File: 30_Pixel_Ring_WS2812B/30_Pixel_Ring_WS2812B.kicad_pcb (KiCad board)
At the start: 2 copper layers, 87.6 x 87.6 mm, 66 parts, among them P1 CONN_01X01, P2 CONN_01X01, P3 CONN_01X01, P4 CONN_01X01, P5 CONN_01X01, P6 CONN_01X01

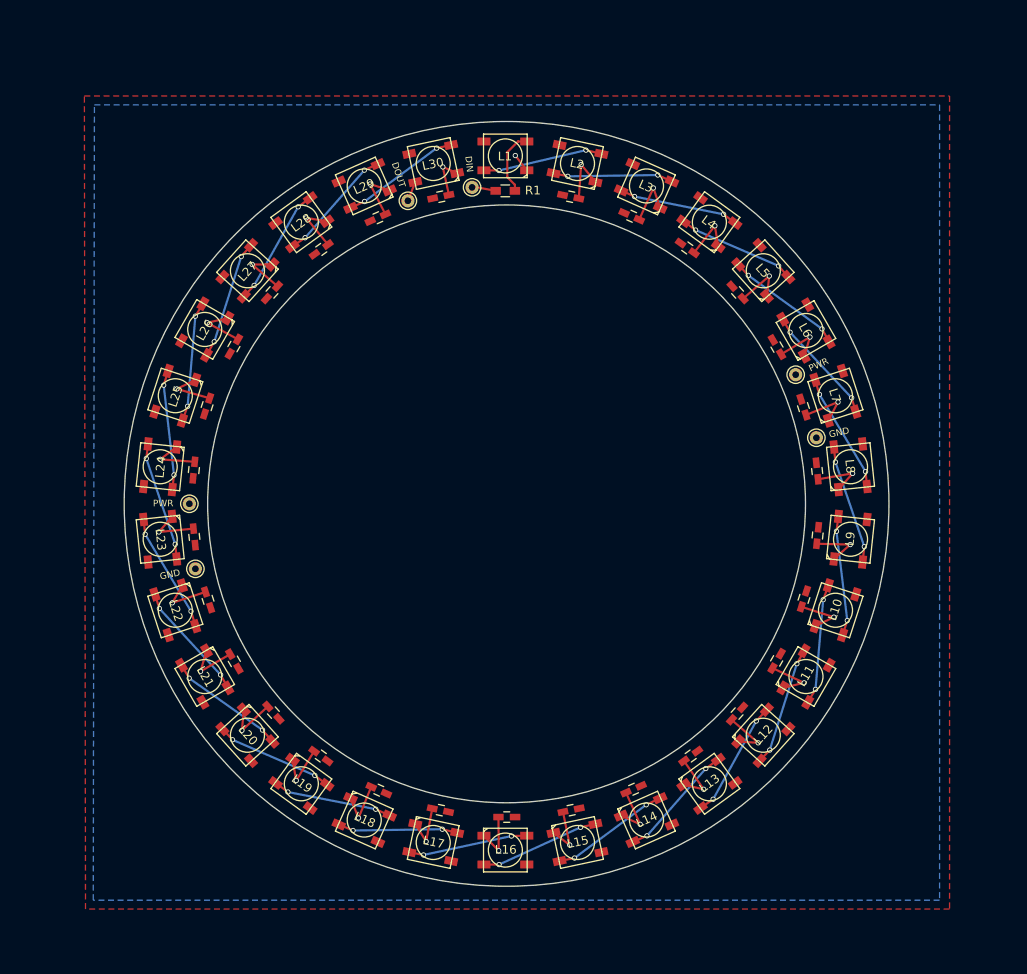
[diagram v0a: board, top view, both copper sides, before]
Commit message: 30 Pixel ring updates
Updates / refinements in preparation for nesting this ring around the 20
pixel ring and sending for fabrication through OSH Park
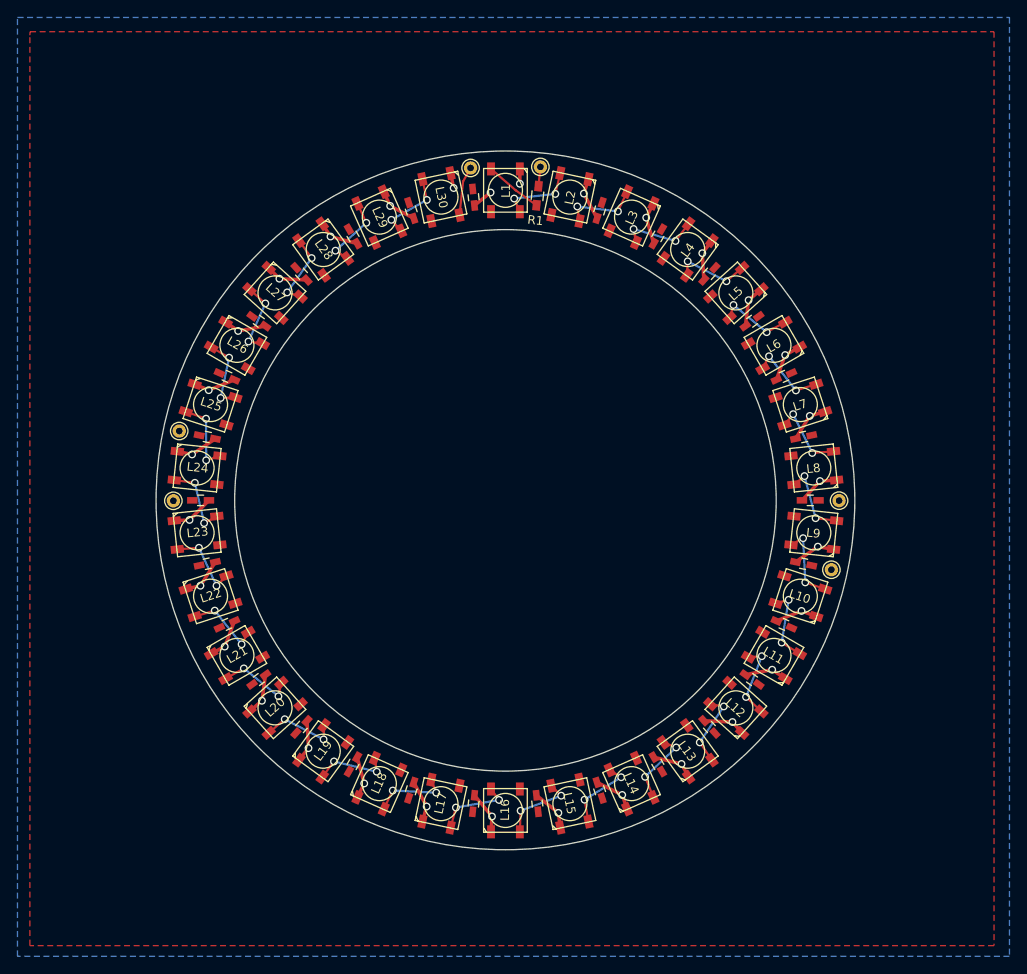
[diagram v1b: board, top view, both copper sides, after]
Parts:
- moved P4 15.3 mm to (216.2, 75.0)
- moved P5 15.2 mm to (215.3, 82.9)
- moved P1 8.41 mm to (140.7, 67.1)
- moved P3 8.19 mm to (140.0, 75.0)
- moved P2 8.16 mm to (182.0, 36.8)
- moved P6 8.10 mm to (174.0, 36.9)
- moved L16 4.54 mm to (178.0, 110.5), turned to 270 degrees
- moved L17 4.53 mm to (170.6, 109.7), turned to 258 degrees
- moved L15 4.53 mm to (185.4, 109.7), turned to 282 degrees
- moved L18 4.51 mm to (163.6, 107.4), turned to 246 degrees
- moved L14 4.51 mm to (192.4, 107.4), turned to 294 degrees
- moved L19 4.49 mm to (157.1, 103.7), turned to 234 degrees
- moved L13 4.48 mm to (198.9, 103.7), turned to 306 degrees
- moved L20 4.45 mm to (151.6, 98.8), turned to 222 degrees
- moved L12 4.44 mm to (204.4, 98.8), turned to 318 degrees
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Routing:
- net GND: track 184.5 -> 143.5 mm, vias 30 -> 31
- net Net-(L23-Pad2): track 13.7 -> 8.76 mm
- net Net-(L25-Pad2): track 13.8 -> 8.79 mm
- net Net-(L29-Pad2): track 13.7 -> 8.77 mm
- net Net-(L1-Pad2): track 13.8 -> 8.82 mm
- net Net-(L5-Pad2): track 13.8 -> 8.88 mm
- net Net-(L18-Pad2): track 13.8 -> 8.83 mm
- net Net-(L28-Pad2): track 13.7 -> 8.82 mm
- net Net-(L2-Pad2): track 13.8 -> 8.85 mm
- net Net-(L26-Pad2): track 13.7 -> 8.84 mm
- net Net-(L24-Pad2): track 13.7 -> 8.86 mm
- net Net-(L22-Pad2): track 13.7 -> 8.89 mm
- net Net-(L27-Pad2): track 13.7 -> 8.89 mm
- net Net-(L21-Pad2): track 13.7 -> 8.91 mm
- net Net-(L10-Pad2): track 13.8 -> 8.94 mm
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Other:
- board size 87.6 x 87.6 mm -> 80 x 80 mm
- net class Default: via_dia 0.6 -> 0.9; via_drill 0.4 -> 0.6
- net class Ground added: clearance 0.2, trace_width 0.4, via_dia 0.9, via_drill 0.6
- net class Power added: clearance 0.2, trace_width 0.4, via_dia 0.9, via_drill 0.6
- rule trace_min: 0.2 -> 0.2032
- rule via_min_drill: 0.3 -> 0.508
- rule via_min_size: 0.4 -> 0.889
- board text added: "10mm width line Outer diameter to inner"
- board text added: "20 Pixel Ring Outer Diameter Ghost"
- board text added: "Circle Center: (178, 75) Ring Outer Diameter: 40 mm Ring Inner Diameter: 30 mm"
- board text added: "Rev: 1B"
- board text removed: "Rev: 1A"
